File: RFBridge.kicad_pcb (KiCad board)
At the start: 4 copper layers, 21 parts

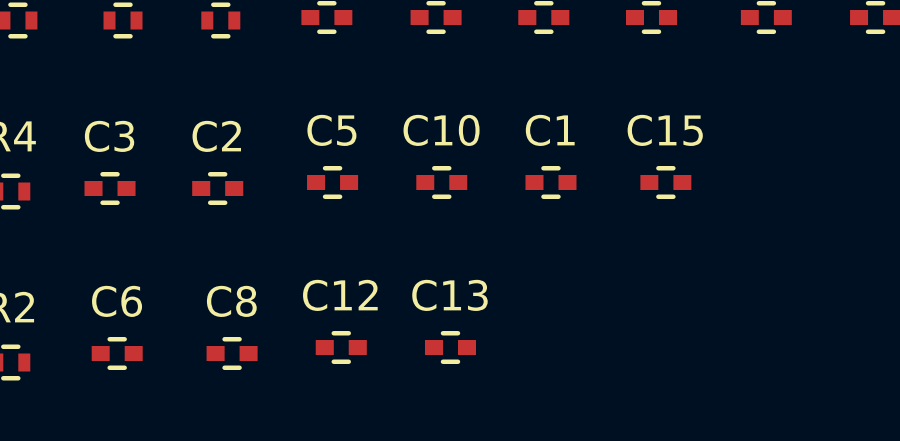
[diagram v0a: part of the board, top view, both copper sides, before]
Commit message: Updated library references
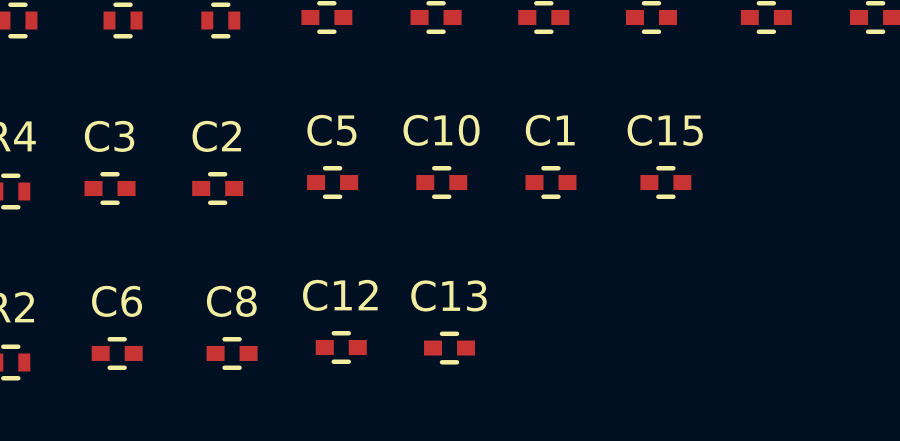
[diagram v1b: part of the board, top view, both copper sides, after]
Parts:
- C1, C10, C11, C12, C13, C14, C15, C16, C2, C3, C4, C5, C6, C7, C8, C9: footprint Passives:C_0402 -> Capacitors_SMD:C_0402
- R1, R2, R3, R4, R5: footprint Passives:R_0402 -> Resistors_SMD:R_0402

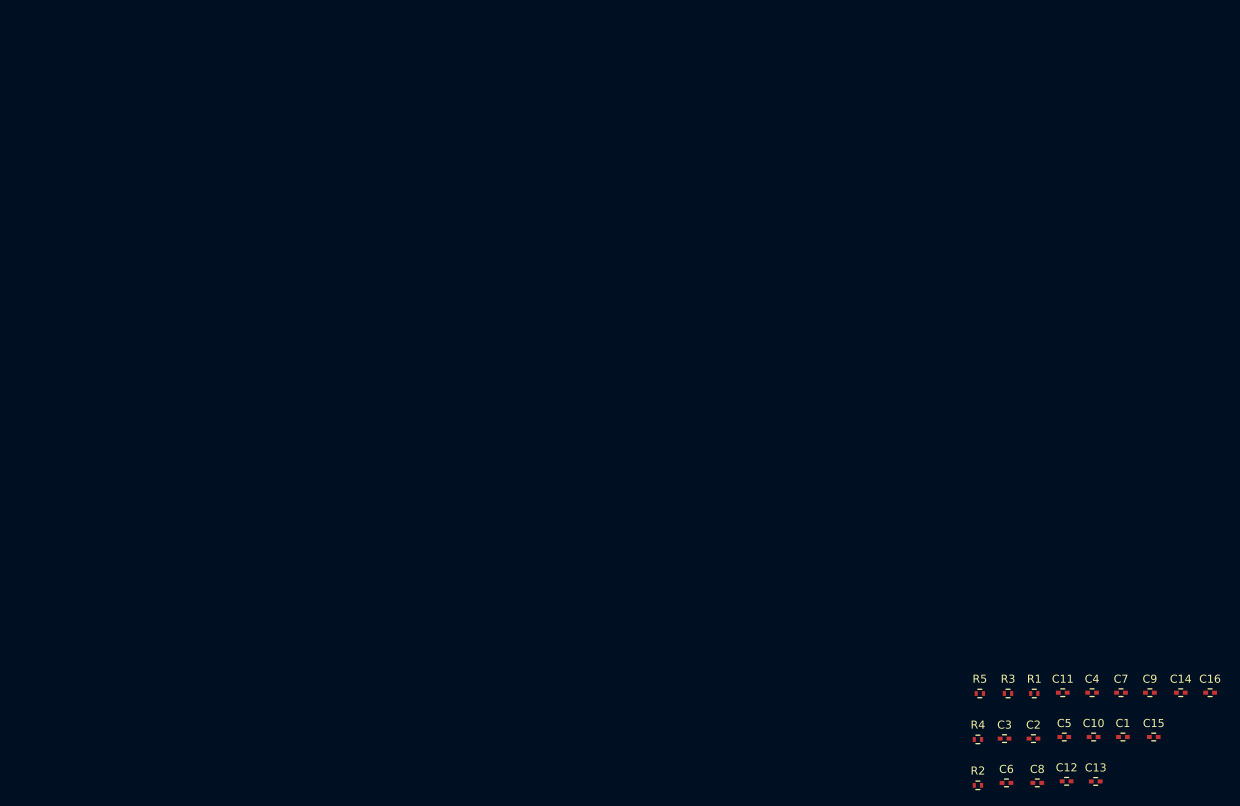
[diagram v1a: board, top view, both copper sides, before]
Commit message: added some radio components.
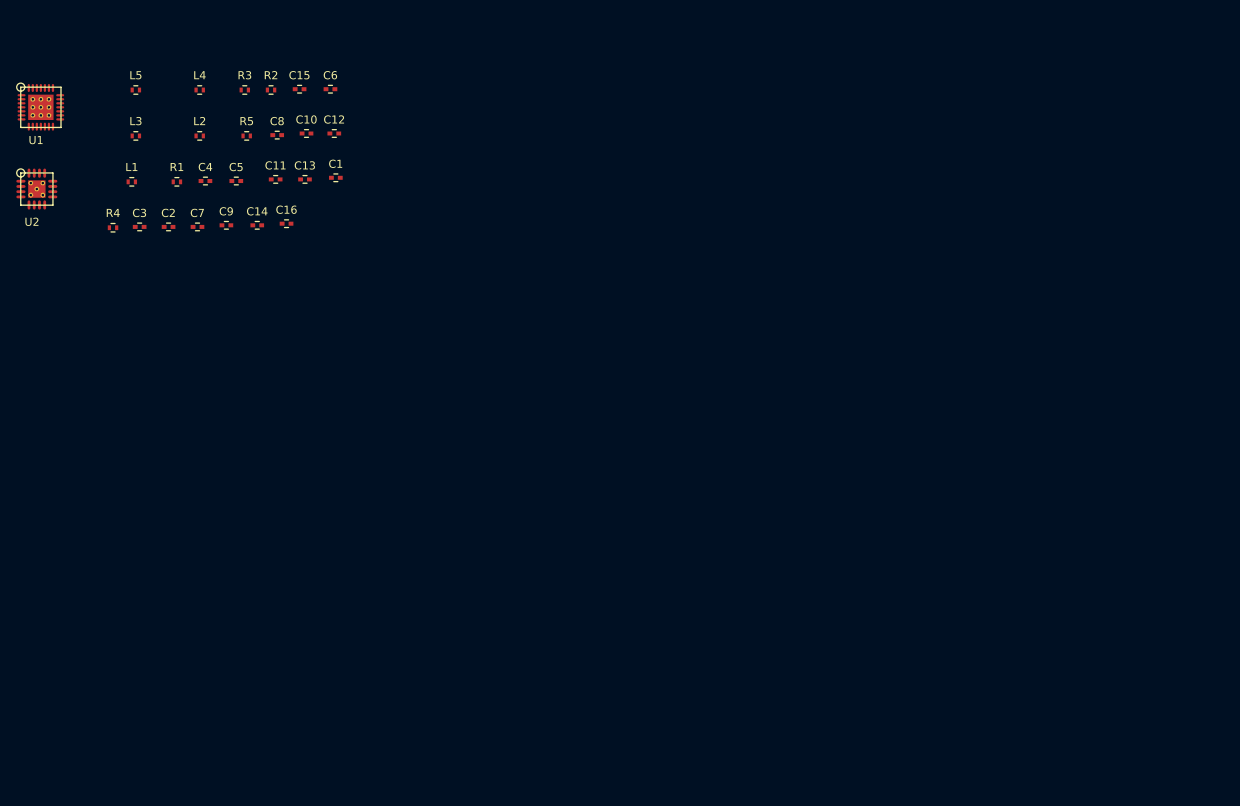
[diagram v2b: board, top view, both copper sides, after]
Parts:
- added L1: INDUCTOR, Resistors_SMD:R_0402, F.Cu at (45.2, 44.3)
- added L2: INDUCTOR, Resistors_SMD:R_0402, F.Cu at (53.6, 38.6)
- added L3: INDUCTOR, Resistors_SMD:R_0402, F.Cu at (45.7, 38.6)
- added L4: INDUCTOR, Resistors_SMD:R_0402, F.Cu at (53.6, 32.9)
- added L5: INDUCTOR, Resistors_SMD:R_0402, F.Cu at (45.7, 32.9)
- added U1: CC2520, SMD_Packages:RHD_S-PVQFN-N28, F.Cu at (33.9, 35.0)
- added U2: CC2592, SMD_Packages:RGV_S-PVQFN-N16, F.Cu at (33.4, 45.2)
- moved C15 133.1 mm to (66.0, 32.8)
- moved C16 128.6 mm to (64.4, 49.5)
- moved C14 128.5 mm to (60.7, 49.7)
- moved C9 128.5 mm to (56.9, 49.7)
- moved C7 128.4 mm to (53.3, 49.9)
- moved C4 127.1 mm to (54.3, 44.2)
- moved C3 124.8 mm to (46.1, 49.9)
- moved C2 124.8 mm to (49.7, 49.9)
- moved R4 124.8 mm to (42.8, 50.0)
- moved C8 124.0 mm to (63.2, 38.5)
- moved R1 124.0 mm to (50.8, 44.3)
- moved C5 123.8 mm to (58.1, 44.2)
- moved C13 123.4 mm to (66.7, 44.0)
- moved C10 123.1 mm to (66.9, 38.3)
- moved R2 123.1 mm to (62.5, 32.9)
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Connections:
- C1 pad 1: Net-(C1-Pad1) -> AVDD
- C1 pad 2: Net-(C1-Pad2) -> GND
- C10 pad 2: Net-(C10-Pad2) -> GND
- C11 pad 1: Net-(C11-Pad1) -> Net-(C10-Pad1)
- C11 pad 2: Net-(C11-Pad2) -> GND
- C12 pad 1: Net-(C12-Pad1) -> Net-(C10-Pad1)
- C12 pad 2: Net-(C12-Pad2) -> GND
- C13 pad 2: Net-(C13-Pad2) -> GND
- C14 pad 2: Net-(C14-Pad2) -> GND
- C15 pad 2: Net-(C15-Pad2) -> GND
- C16 pad 2: Net-(C16-Pad2) -> Net-(C15-Pad1)
- C2 pad 1: Net-(C2-Pad1) -> AVDD
- C2 pad 2: Net-(C2-Pad2) -> GND
- C3 pad 2: Net-(C3-Pad2) -> GND
- C4 pad 1: Net-(C4-Pad1) -> AVDD
- C4 pad 2: Net-(C4-Pad2) -> GND
- C5 pad 1: Net-(C5-Pad1) -> AVDD
- C5 pad 2: Net-(C5-Pad2) -> GND
- C6 pad 2: Net-(C6-Pad2) -> GND
- C7 pad 2: Net-(C7-Pad2) -> GND
- C8 pad 1: Net-(C8-Pad1) -> Net-(C10-Pad1)
- C8 pad 2: Net-(C8-Pad2) -> GND
- C9 pad 1: Net-(C9-Pad1) -> GND
- R1 pad 2: Net-(R1-Pad2) -> GND
- R5 pad 2: Net-(R5-Pad2) -> GND

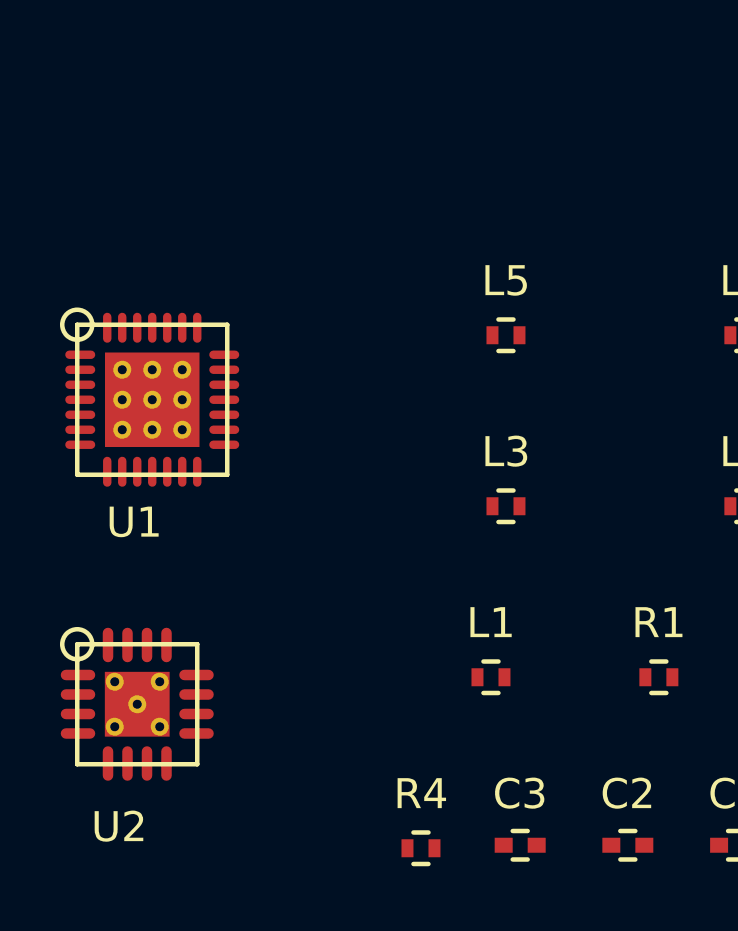
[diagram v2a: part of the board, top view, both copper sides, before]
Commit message: Added more RF components
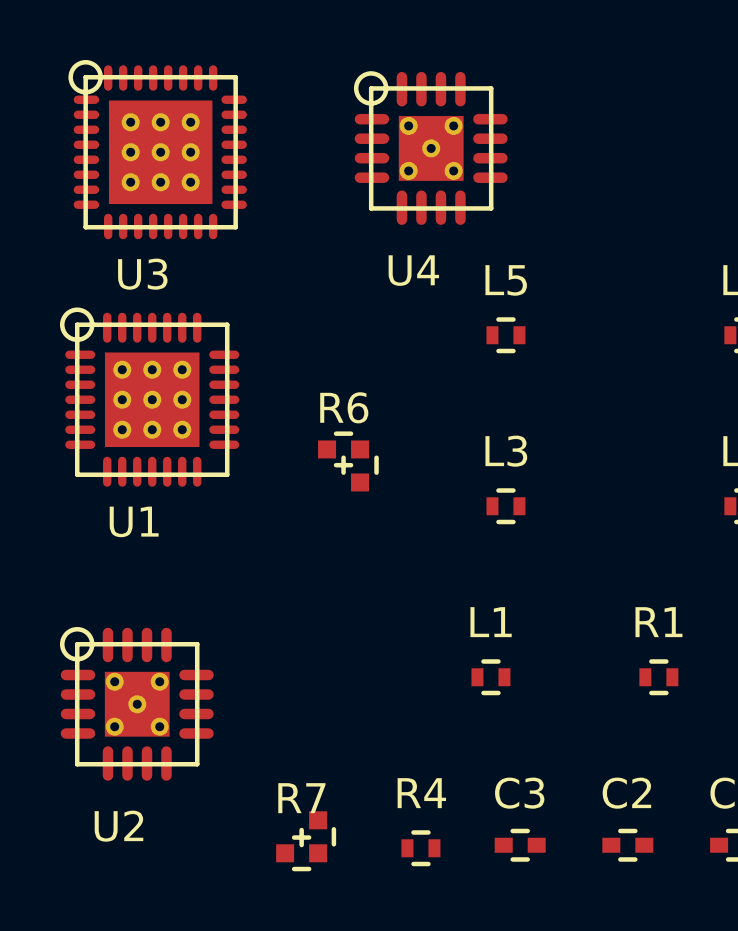
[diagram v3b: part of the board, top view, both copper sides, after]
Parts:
- added R6: R3-RH, Resistors_SMD:R3_RH_0402, F.Cu at (40.3, 36.7)
- added R7: R3-LH, Resistors_SMD:R3_LH_0402, F.Cu at (38.9, 50.2)
- added U3: CC1120, SMD_Packages:RHB_S-PVQFN-N32, F.Cu at (34.2, 26.8)
- added U4: CC1190, SMD_Packages:RGV_S-PVQFN-N16, F.Cu at (43.2, 26.7)

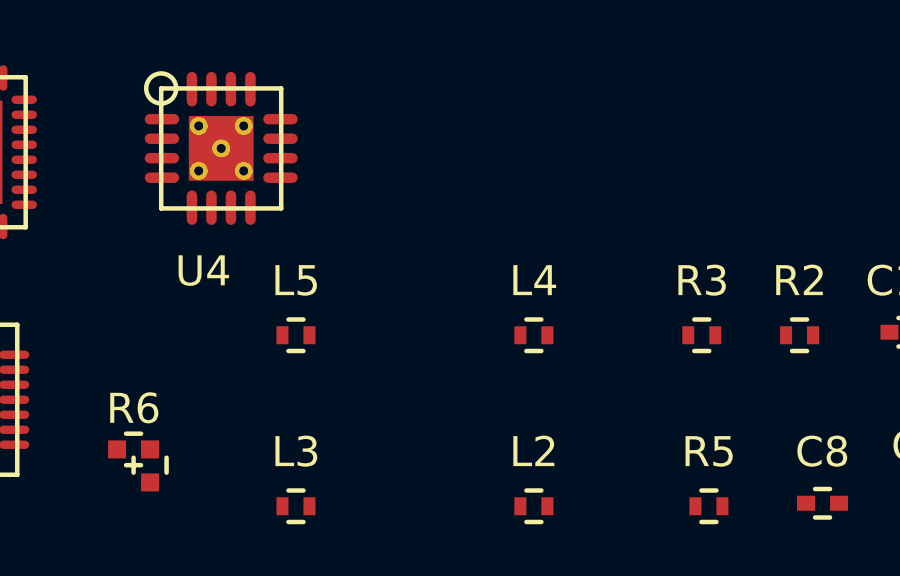
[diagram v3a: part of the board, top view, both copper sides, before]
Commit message: Added baluns
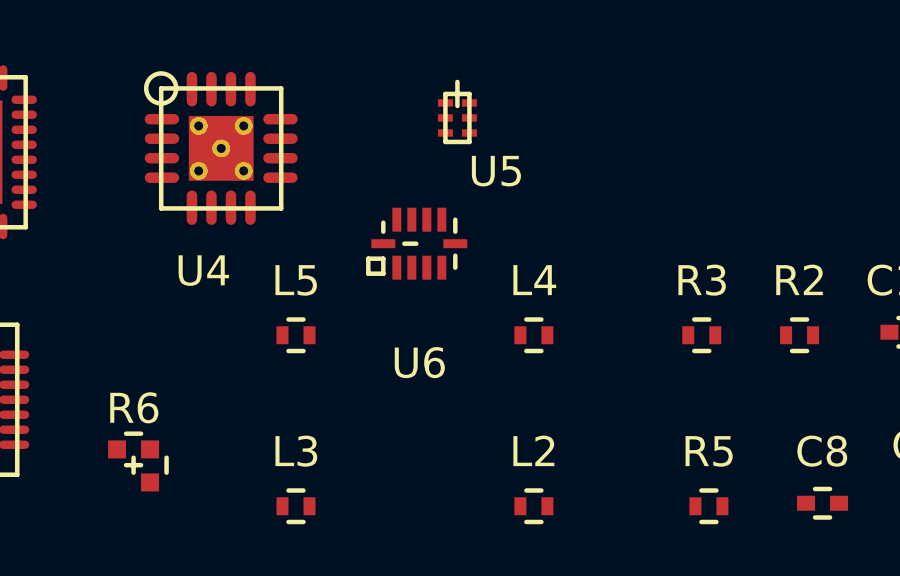
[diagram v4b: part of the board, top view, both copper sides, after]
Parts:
- added U5: LDB182G4520C-110, SMD_Packages:LDB18, F.Cu at (51.1, 25.7)
- added U6: 0900PC15J0013, SMD_Packages:0900PC15J0013, F.Cu at (49.8, 29.8)
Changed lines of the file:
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@@
 (kicad_pcb (version 4) (host pcbnew "(2015-07-02 BZR 5871)-product")
   (general
-    (links 112)
-    (no_connects 84)
+    (links 115)
+    (no_connects 87)
     (area 30.607 21.595 72.422714 52.94)
     (thickness 1.6)
@@
     (tracks 0)
     (zones 0)
-    (modules 32)
-    (nets 86)
+    (modules 34)
+    (nets 99)
   )
   (page A4)
@@
   (net 84 "Net-(U4-Pad15)")
   (net 85 "Net-(U4-Pad16)")
+  (net 86 "Net-(U5-Pad1)")
+  (net 87 "Net-(U5-Pad2)")
+  (net 88 "Net-(U5-Pad5)")
+  (net 89 "Net-(U6-Pad10)")
+  (net 90 "Net-(U6-Pad6)")
+  (net 91 "Net-(U6-Pad4)")
+  (net 92 "Net-(U6-Pad1)")
+  (net 93 "Net-(U6-Pad2)")
+  (net 94 "Net-(U6-Pad3)")
+  (net 95 "Net-(U6-Pad5)")
+  (net 96 "Net-(U6-Pad7)")
+  (net 97 "Net-(U6-Pad8)")
+  (net 98 "Net-(U6-Pad9)")
   (net_class Default "This is the default net class."
     (clearance 0.2)
@@
     (add_net "Net-(U4-Pad7)")
     (add_net "Net-(U4-Pad8)")
+    (add_net "Net-(U5-Pad1)")
+    (add_net "Net-(U5-Pad2)")
+    (add_net "Net-(U5-Pad5)")
+    (add_net "Net-(U6-Pad1)")
+    (add_net "Net-(U6-Pad10)")
+    (add_net "Net-(U6-Pad2)")
+    (add_net "Net-(U6-Pad3)")
+    (add_net "Net-(U6-Pad4)")
+    (add_net "Net-(U6-Pad5)")
+    (add_net "Net-(U6-Pad6)")
+    (add_net "Net-(U6-Pad7)")
+    (add_net "Net-(U6-Pad8)")
+    (add_net "Net-(U6-Pad9)")
   )
   (module Capacitors_SMD:C_0402 (layer F.Cu)
@@
       (at (xyz 0 0 0))
       (scale (xyz 1 1 1))
+      (rotate (xyz 0 0 0))
+    )
+  )
+  (module SMD_Packages:LDB18 (layer F.Cu)
+    (at 51.054 25.654)
+    (fp_text reference U5 (at 1.3 1.8) (layer F.SilkS)
+      (effects (font (size 1 1) (thickness 0.15)))
+    )
+    (fp_text value LDB182G4520C-110 (at 1.5 -1.9) (layer F.Fab)
+      (effects (font (size 1 1) (thickness 0.15)))
+    )
+    (fp_line (start 0 -0.4) (end 0 -1.2) (layer F.SilkS) (width 0.15))
+    (fp_line (start -0.4 -0.8) (end -0.4 0.8) (layer F.SilkS) (width 0.15))
+    (fp_line (start -0.4 0.8) (end 0.4 0.8) (layer F.SilkS) (width 0.15))
+    (fp_line (start 0.4 0.8) (end 0.4 -0.8) (layer F.SilkS) (width 0.15))
+    (fp_line (start 0.4 -0.8) (end -0.4 -0.8) (layer F.SilkS) (width 0.15))
+    (pad 1 smd rect (at -0.4 -0.5) (size 0.5 0.25) (layers F.Cu F.Paste F.Mask)
+      (net 86 "Net-(U5-Pad1)"))
+    (pad 2 smd rect (at -0.4 0) (size 0.5 0.25) (layers F.Cu F.Paste F.Mask)
+      (net 87 "Net-(U5-Pad2)"))
+    (pad 3 smd rect (at -0.4 0.5) (size 0.5 0.25) (layers F.Cu F.Paste F.Mask)
+      (net 4 "Net-(C9-Pad2)"))
+    (pad 4 smd rect (at 0.4 0.5) (size 0.5 0.25) (layers F.Cu F.Paste F.Mask)
+      (net 39 "Net-(R7-Pad3)"))
+    (pad 5 smd rect (at 0.4 0) (size 0.5 0.25) (layers F.Cu F.Paste F.Mask)
+      (net 88 "Net-(U5-Pad5)"))
+    (pad 6 smd rect (at 0.4 -0.5) (size 0.5 0.25) (layers F.Cu F.Paste F.Mask)
+      (net 36 "Net-(R6-Pad3)"))
+    (model SMD_Packages.3dshapes/LDB18.wrl
+      (at (xyz 0 0 0))
+      (scale (xyz 1 1 1))
+      (rotate (xyz 0 0 0))
+    )
+  )
+  (module SMD_Packages:0900PC15J0013 (layer F.Cu)
+    (at 49.784 29.845)
+    (fp_text reference U6 (at 0 4) (layer F.SilkS)
+      (effects (font (size 1 1) (thickness 0.15)))
+    )
+    (fp_text value 0900PC15J0013 (at 0 -4.2) (layer F.Fab)
+      (effects (font (size 1 1) (thickness 0.15)))
+    )
+    (fp_line (start 1.2 0.4) (end 1.2 0.8) (layer F.SilkS) (width 0.15))
+    (fp_line (start 1.2 -0.4) (end 1.2 -0.8) (layer F.SilkS) (width 0.15))
+    (fp_line (start -1.2 -0.4) (end -1.2 -0.7) (layer F.SilkS) (width 0.15))
+    (fp_line (start -0.5 0) (end -0.1 0) (layer F.SilkS) (width 0.15))
+    (fp_line (start -1.2 0.5) (end -1.2 1) (layer F.SilkS) (width 0.15))
+    (fp_line (start -1.2 1) (end -1.7 1) (layer F.SilkS) (width 0.15))
+    (fp_line (start -1.7 1) (end -1.7 0.5) (layer F.SilkS) (width 0.15))
+    (fp_line (start -1.7 0.5) (end -1.2 0.5) (layer F.SilkS) (width 0.15))
+    (pad 10 smd rect (at -1.2 0 180) (size 0.8 0.3) (layers F.Cu F.Paste F.Mask)
+      (net 89 "Net-(U6-Pad10)"))
+    (pad 6 smd rect (at 0.75 -0.8 270) (size 0.8 0.3) (layers F.Cu F.Paste F.Mask)
+      (net 90 "Net-(U6-Pad6)"))
+    (pad 4 smd rect (at 0.75 0.8 90) (size 0.8 0.3) (layers F.Cu F.Paste F.Mask)
+      (net 91 "Net-(U6-Pad4)"))
+    (pad 1 smd rect (at -0.75 0.8 90) (size 0.8 0.3) (layers F.Cu F.Paste F.Mask)
+      (net 92 "Net-(U6-Pad1)"))
+    (pad 2 smd rect (at -0.25 0.8 90) (size 0.8 0.3) (layers F.Cu F.Paste F.Mask)
+      (net 93 "Net-(U6-Pad2)"))
+    (pad 3 smd rect (at 0.25 0.8 90) (size 0.8 0.3) (layers F.Cu F.Paste F.Mask)
+      (net 94 "Net-(U6-Pad3)"))
+    (pad 5 smd rect (at 1.2 0 180) (size 0.8 0.3) (layers F.Cu F.Paste F.Mask)
+      (net 95 "Net-(U6-Pad5)"))
+    (pad 7 smd rect (at 0.25 -0.8 270) (size 0.8 0.3) (layers F.Cu F.Paste F.Mask)
+      (net 96 "Net-(U6-Pad7)"))
+    (pad 8 smd rect (at -0.25 -0.8 270) (size 0.8 0.3) (layers F.Cu F.Paste F.Mask)
+      (net 97 "Net-(U6-Pad8)"))
+    (pad 9 smd rect (at -0.75 -0.8 270) (size 0.8 0.3) (layers F.Cu F.Paste F.Mask)
+      (net 98 "Net-(U6-Pad9)"))
+    (model SMD_Packages.3dshapes/0900PC15J0013.wrl
+      (at (xyz 0 0 0))
+      (scale (xyz 1 1 1))
